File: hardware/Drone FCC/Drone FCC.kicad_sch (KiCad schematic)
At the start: 0 parts

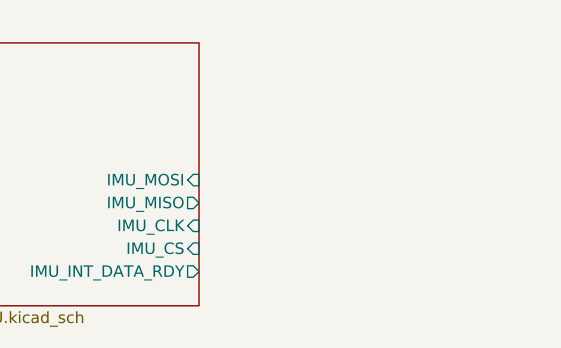
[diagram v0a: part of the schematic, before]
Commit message: esquematico barometro I2C
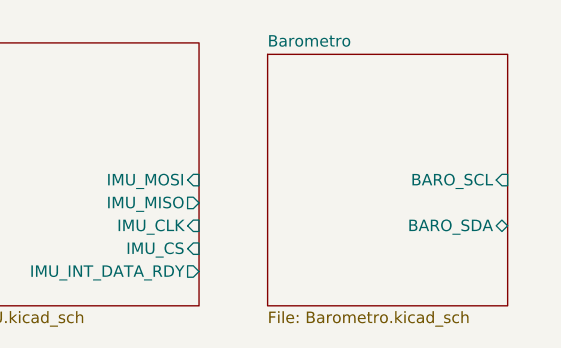
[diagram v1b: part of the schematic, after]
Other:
- added sheet Barometro (Barometro.kicad_sch)
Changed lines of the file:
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@@
 (kicad_sch (version 20211123) (generator eeschema)
   (paper "A4")
+  (sheet (at 99.06 21.59) (size 26.67 27.94) (fields_autoplaced)
+    (stroke (width 0.1524) (type solid) (color 0 0 0 0))
+    (fill (color 0 0 0 0.0000))
+    (property "Sheet name" "Barometro" (id 0) (at 99.06 20.8784 0)
+      (effects (font (size 1.27 1.27)) (justify left bottom))
+    )
+    (property "Sheet file" "Barometro.kicad_sch" (id 1) (at 99.06 50.1146 0)
+      (effects (font (size 1.27 1.27)) (justify left top))
+    )
+    (pin "BARO_SCL" input (at 125.73 35.56 0)
+      (effects (font (size 1.27 1.27)) (justify right))
+    )
+    (pin "BARO_SDA" bidirectional (at 125.73 40.64 0)
+      (effects (font (size 1.27 1.27)) (justify right))
+    )
+  )
   (sheet (at 62.23 20.32) (size 29.21 29.21) (fields_autoplaced)
     (stroke (width 0.1524) (type solid) (color 0 0 0 0))
@@
     (path "/" (page "1"))
     (path "/0ee7de47-20c2-4341-81cd-1c3f43cc8a34" (page "2"))
+    (path "/0a0aeaa0-9fdf-480f-a2c4-a3ed4cfe4b7a" (page "3"))
   )
   (symbol_instances
@@
       (reference "#PWR05") (unit 1) (value "GND") (footprint "")
     )
+    (path "/0a0aeaa0-9fdf-480f-a2c4-a3ed4cfe4b7a/10efe182-945f-4d56-a3e4-2e3089e4e28f"
+      (reference "#PWR?") (unit 1) (value "GND") (footprint "")
+    )
+    (path "/0a0aeaa0-9fdf-480f-a2c4-a3ed4cfe4b7a/24bc73d4-61db-4b6c-aef0-b2d81767b669"
+      (reference "#PWR?") (unit 1) (value "GND") (footprint "")
+    )
+    (path "/0a0aeaa0-9fdf-480f-a2c4-a3ed4cfe4b7a/62a5f455-4451-43d5-a9e8-4fa38575ef6c"
+      (reference "#PWR?") (unit 1) (value "GND") (footprint "")
+    )
     (path "/0ee7de47-20c2-4341-81cd-1c3f43cc8a34/1acf1ca3-aaf6-4369-a9f9-ef4d47a00c4a"
-      (reference "C1") (unit 1) (value "0.10uF") (footprint "")
+      (reference "C1") (unit 1) (value "100n") (footprint "")
     )
     (path "/0ee7de47-20c2-4341-81cd-1c3f43cc8a34/93528709-610a-4ffe-a7ef-fc87f8cedaa4"
-      (reference "C2") (unit 1) (value "2.2uF") (footprint "")
+      (reference "C2") (unit 1) (value "2.2u") (footprint "")
     )
     (path "/0ee7de47-20c2-4341-81cd-1c3f43cc8a34/4f25d9d8-41af-4070-b19d-a83da8ddd106"
-      (reference "C3") (unit 1) (value "10nF") (footprint "")
+      (reference "C3") (unit 1) (value "10n") (footprint "")
+    )
+    (path "/0a0aeaa0-9fdf-480f-a2c4-a3ed4cfe4b7a/50175427-1b07-436b-bc8d-cb51dd9cff8f"
+      (reference "C?") (unit 1) (value "4.7u") (footprint "")
+    )
+    (path "/0a0aeaa0-9fdf-480f-a2c4-a3ed4cfe4b7a/815e1bf9-e1ca-4561-b37d-c11bdf78b781"
+      (reference "C?") (unit 1) (value "100n") (footprint "")
     )
     (path "/0ee7de47-20c2-4341-81cd-1c3f43cc8a34/13e9cb4a-612d-4494-b4d3-c996fd15ec9d"
@@
       (reference "R2") (unit 1) (value "R") (footprint "")
     )
+    (path "/0a0aeaa0-9fdf-480f-a2c4-a3ed4cfe4b7a/751f292a-e99e-4321-970e-7419a0390e72"
+      (reference "R?") (unit 1) (value "R") (footprint "")
+    )
+    (path "/0a0aeaa0-9fdf-480f-a2c4-a3ed4cfe4b7a/8a584082-9e74-406b-b17d-56448ae67c81"
+      (reference "R?") (unit 1) (value "R") (footprint "")
+    )
+    (path "/0a0aeaa0-9fdf-480f-a2c4-a3ed4cfe4b7a/a65f3764-3b76-4212-bfa2-b65823fbc2ce"
+      (reference "R?") (unit 1) (value "R") (footprint "")
+    )
+    (path "/0a0aeaa0-9fdf-480f-a2c4-a3ed4cfe4b7a/eff94eaf-f3ca-4217-8f58-02be6b3bb012"
+      (reference "R?") (unit 1) (value "R") (footprint "")
+    )
     (path "/0ee7de47-20c2-4341-81cd-1c3f43cc8a34/c0a47081-331a-4786-8c58-279f979e2a17"
       (reference "U1") (unit 1) (value "ICM-42688-P") (footprint "PQFN50P300X250X97-14N")
     )
+    (path "/0a0aeaa0-9fdf-480f-a2c4-a3ed4cfe4b7a/bfa78c7d-fb84-460e-886c-6bf899fd0853"
+      (reference "U?") (unit 1) (value "ILPS22QSTR") (footprint "HLGA_10L_STM")
+    )
   )

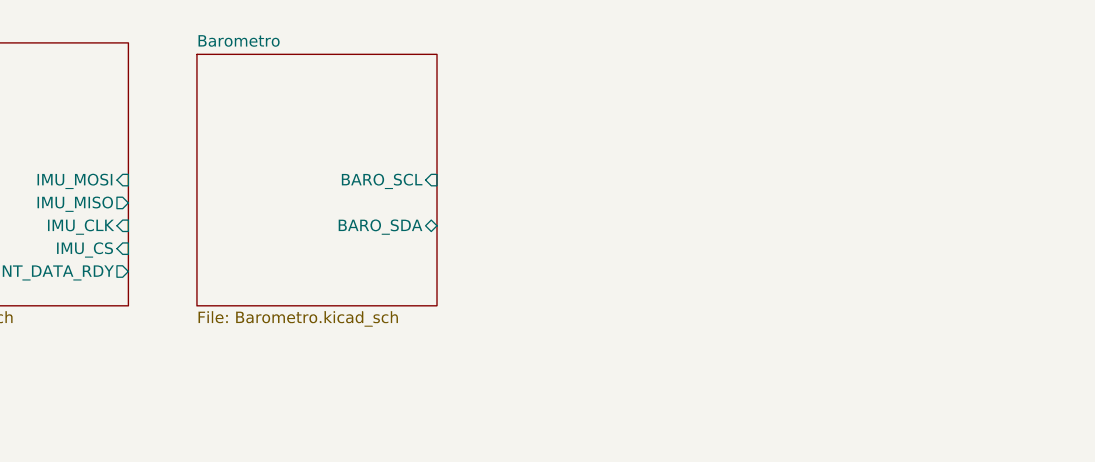
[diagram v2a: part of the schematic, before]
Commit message: add connectors for PWM
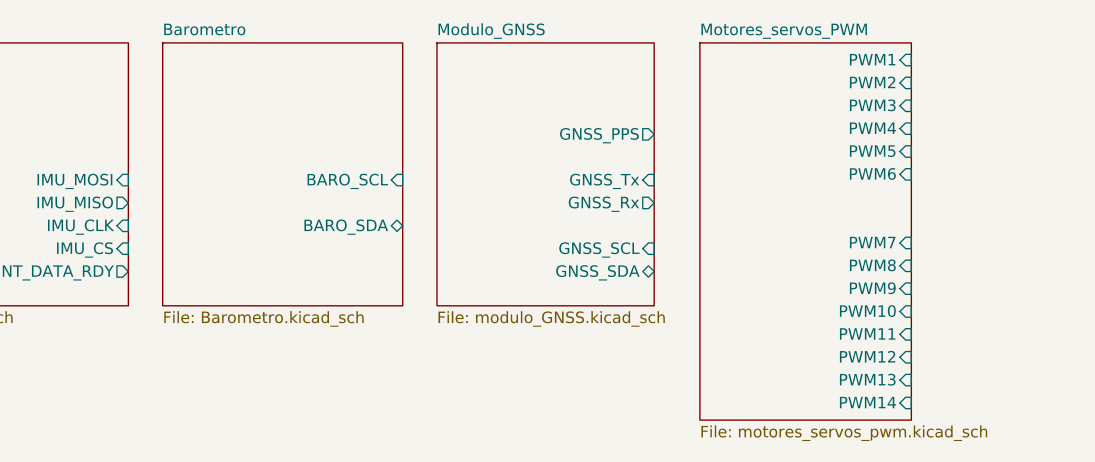
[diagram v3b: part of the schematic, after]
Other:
- added sheet Modulo_GNSS (modulo_GNSS.kicad_sch)
- added sheet Motores_servos_PWM (motores_servos_pwm.kicad_sch)

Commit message: started schematic
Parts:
- added U3: STM32F746ZGTx, Package_QFP:LQFP-144_20x20mm_P0.5mm, symbol MCU_ST_STM32F7:STM32F746ZGTx
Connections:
- new net I2C1_SCL: U3.140 (PB9)
- new net I2C1_SDA: U3.139 (PB8)
- new net I2C2_SCL: U3.11 (PF1)
- new net I2C2_SDA: U3.10 (PF0)
- new net I2C3_SCL: U3.100 (PA8)
- new net I2C3_SDA: U3.99 (PC9)
- new net I2C4_SCL: U3.54 (PF14)
- new net I2C4_SDA: U3.55 (PF15)
- new net IMU_MISO: U3.42 (PA6)
- new net IMU_MOSI: U3.43 (PA7)
- new net IMU_SCK: U3.41 (PA5)
- new net PWM1: U3.81 (PD12)
- new net PWM2: U3.82 (PD13)
- new net PWM3: U3.85 (PD14)
- new net PWM4: U3.86 (PD15)
- new net PWM5: U3.60 (PE9)
- new net PWM6: U3.64 (PE11)
- new net PWM7: U3.66 (PE13)
- new net PWM8: U3.67 (PE14)
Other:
- added sheet Interfaz_CAN (interfaz_can.kicad_sch)
- sheet Motores_servos_PWM ports: added ESC_1, ESC_2, ESC_3, ESC_4, ESC_5, ESC_6; removed PWM1, PWM2, PWM3, PWM4, PWM5, PWM6

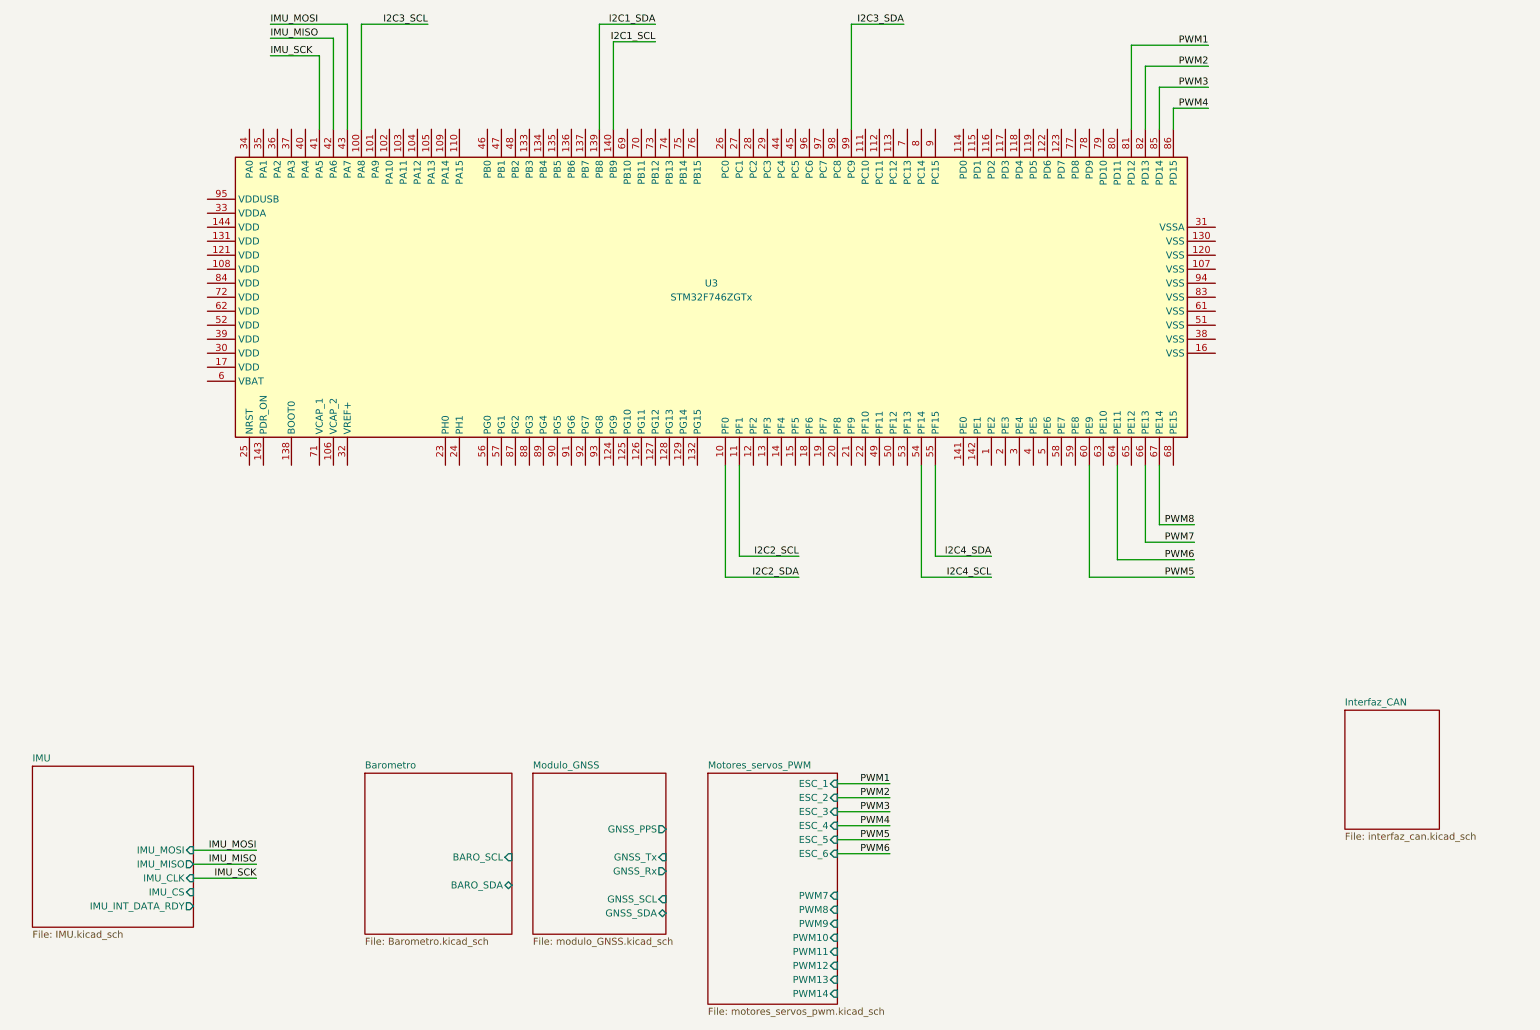
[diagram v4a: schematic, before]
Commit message: all sensors on same schematic subpage
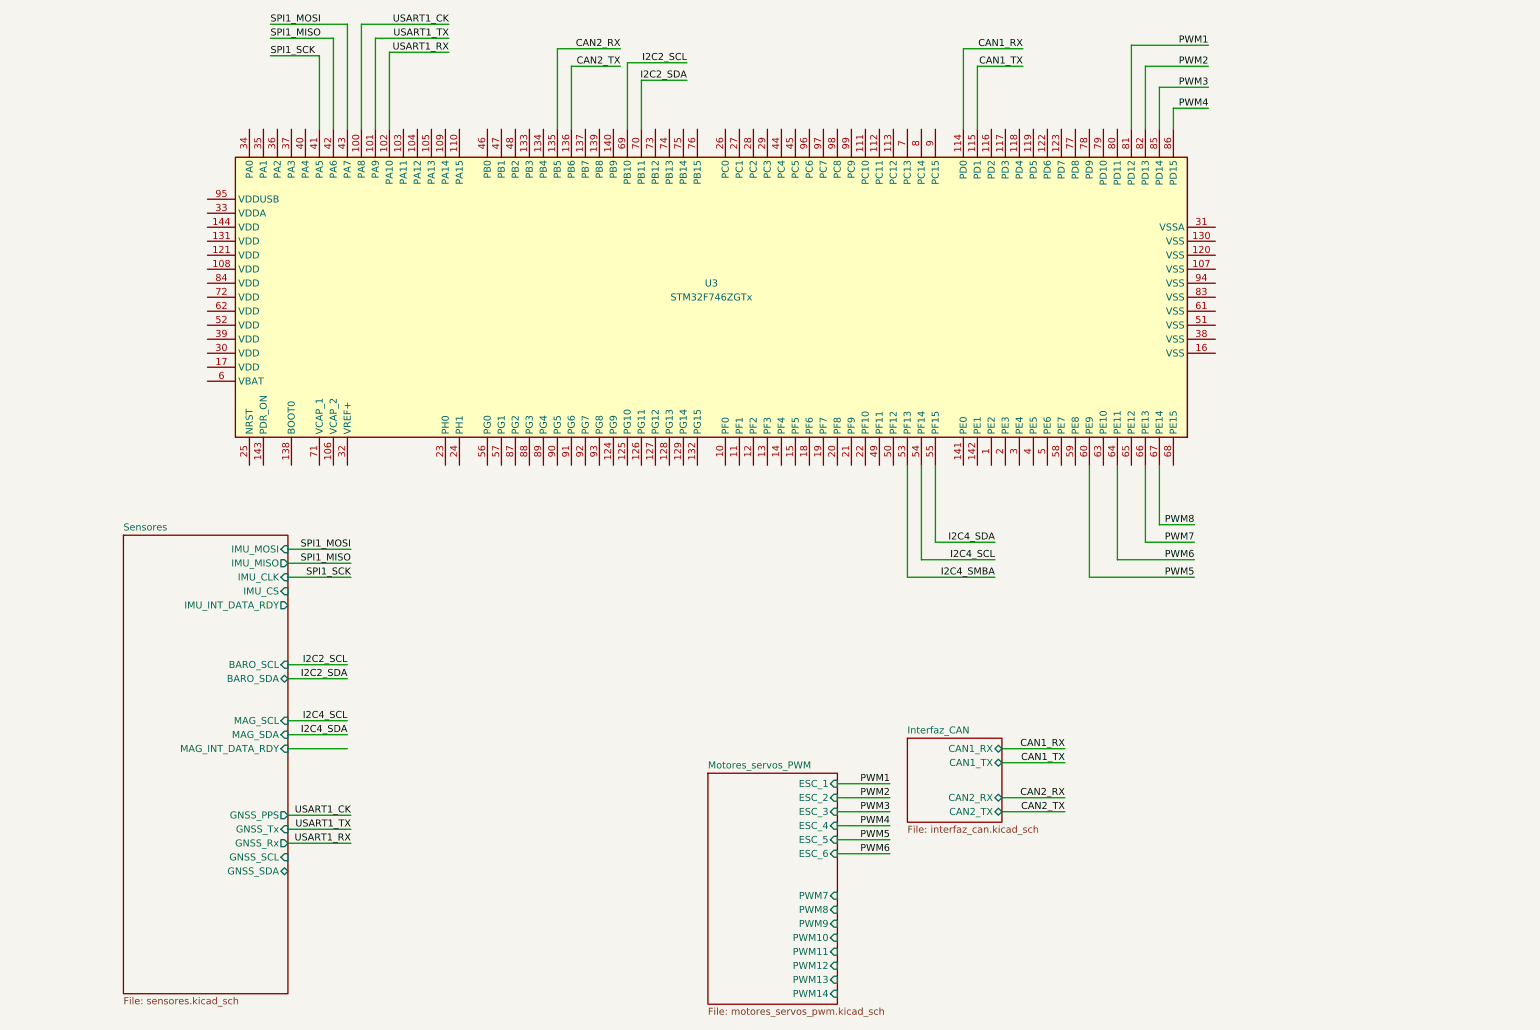
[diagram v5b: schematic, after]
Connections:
- net I2C2_SCL: now also U3.69 (PB10); no longer U3.11 (PF1)
- net I2C2_SDA: now also U3.70 (PB11); no longer U3.10 (PF0)
- net USART1_TX: now reaches U3.101 (PA9)
- net USART1_RX: now reaches U3.102 (PA10)
- net CAN1_RX: now reaches U3.114 (PD0)
- net CAN1_TX: now reaches U3.115 (PD1)
- net CAN2_RX: now reaches U3.135 (PB5)
- net CAN2_TX: now reaches U3.136 (PB6)
- net I2C4_SMBA: now reaches U3.53 (PF13)
- net I2C1_SCL: no longer names the net of U3.140 (PB9)
- net I2C1_SDA: no longer names the net of U3.139 (PB8)
- net I2C3_SCL renamed USART1_CK
- net I2C3_SDA: no longer names the net of U3.99 (PC9)
- net IMU_MISO renamed SPI1_MISO
- net IMU_MOSI renamed SPI1_MOSI
- net IMU_SCK renamed SPI1_SCK
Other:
- removed sheet Barometro
- removed sheet IMU
- removed sheet Modulo_GNSS
- added sheet Sensores (sensores.kicad_sch)
- sheet Interfaz_CAN ports: added CAN1_RX, CAN1_TX, CAN2_RX, CAN2_TX; removed none

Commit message: add USB connector
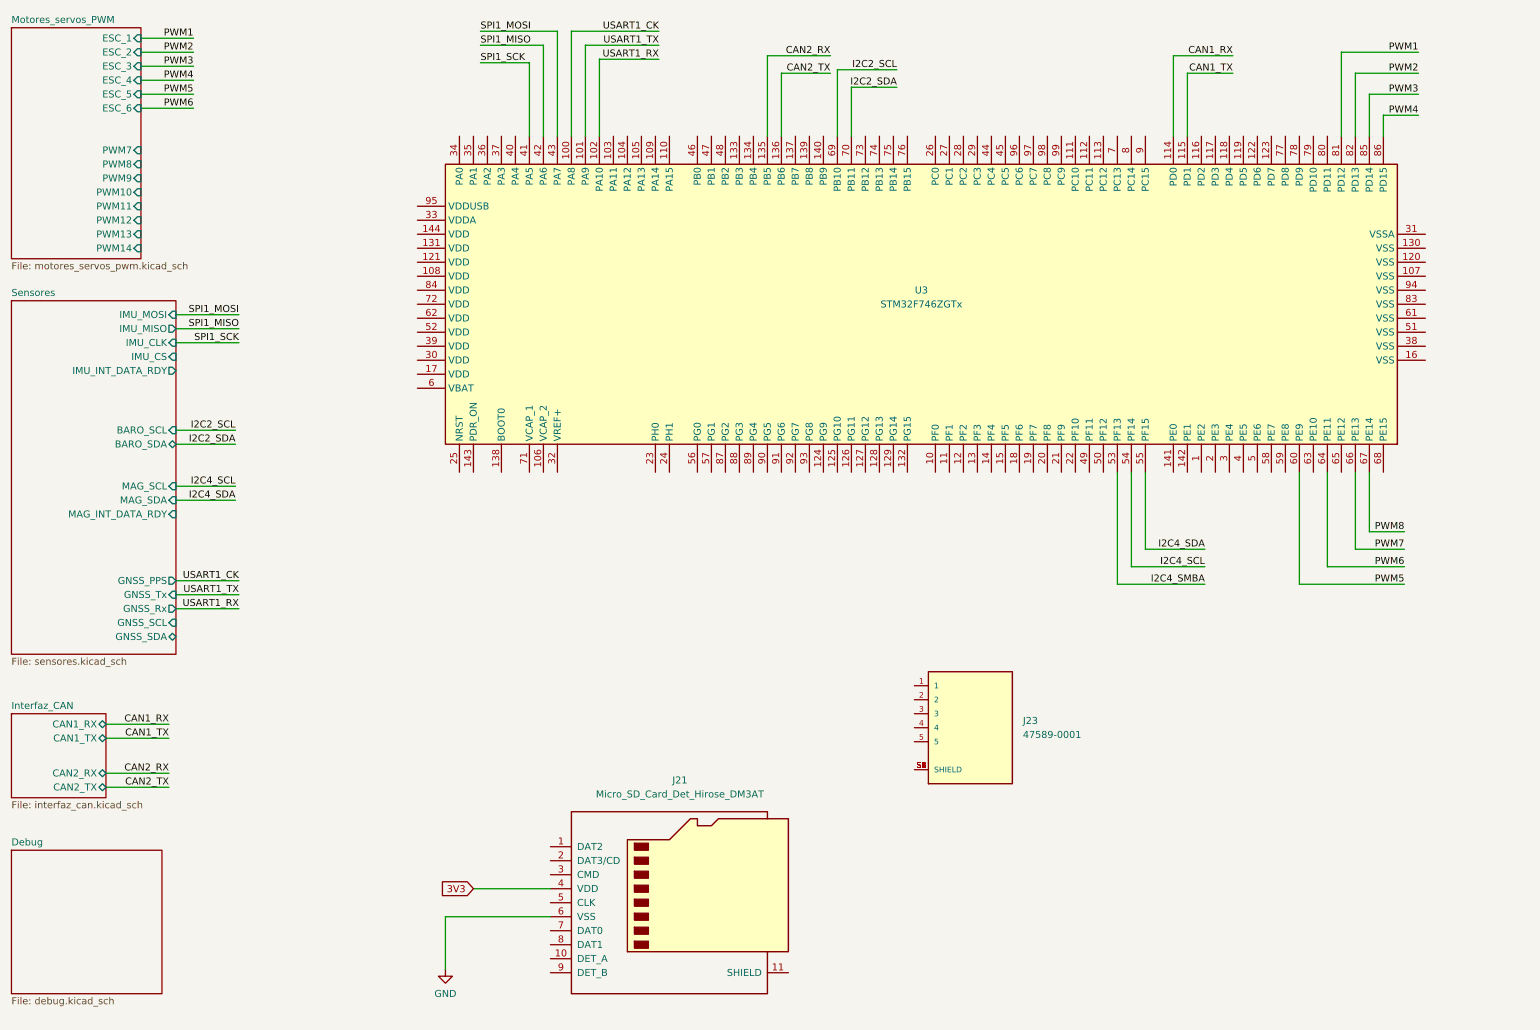
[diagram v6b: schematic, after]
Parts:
- added J21: Micro_SD_Card_Det_Hirose_DM3AT, DM3AT-SF-PEJM5:HRS_DM3AT-SF-PEJM5, symbol Connector:Micro_SD_Card_Det_Hirose_DM3AT
- added J23: 47589-0001, 47589-0001:MOLEX_47589-0001, symbol 47589-0001:47589-0001
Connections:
- new net: J23.S1 (SHIELD), J23.S2 (SHIELD), J23.S3 (SHIELD), J23.S4 (SHIELD), J23.S5 (SHIELD), J23.S6 (SHIELD)
- new net 3V3: J21.4 (VDD)
- new net GND: J21.6 (VSS)
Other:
- added sheet Debug (debug.kicad_sch)
- moved on the sheet: U3
